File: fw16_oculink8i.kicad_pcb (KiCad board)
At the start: 4 copper layers, 118.7 x 72.5 mm, 18 parts, among them J1 173162-0131, J3 Fan0, J4 Fan1, U1 BR24G32FVT-3GE2

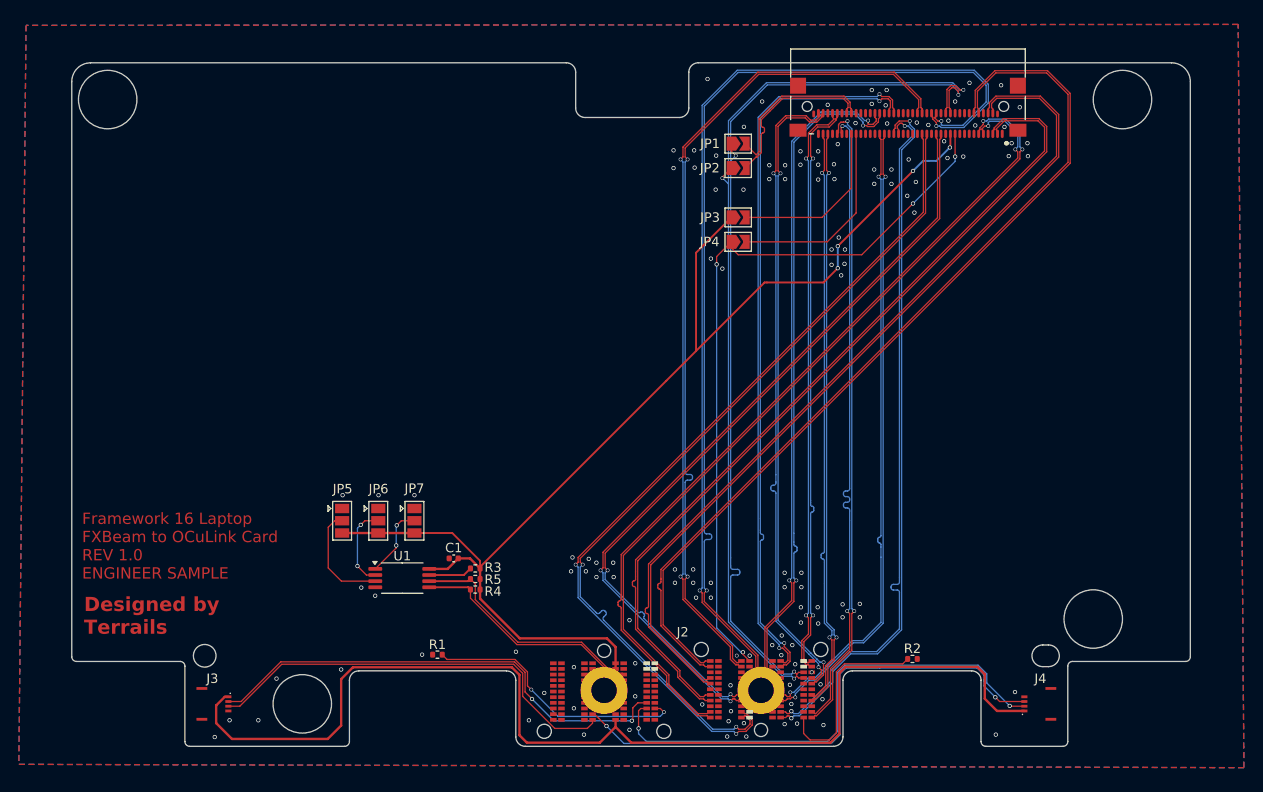
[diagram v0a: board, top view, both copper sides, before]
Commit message: Switch to 0R resistor rather than jumper solder pads
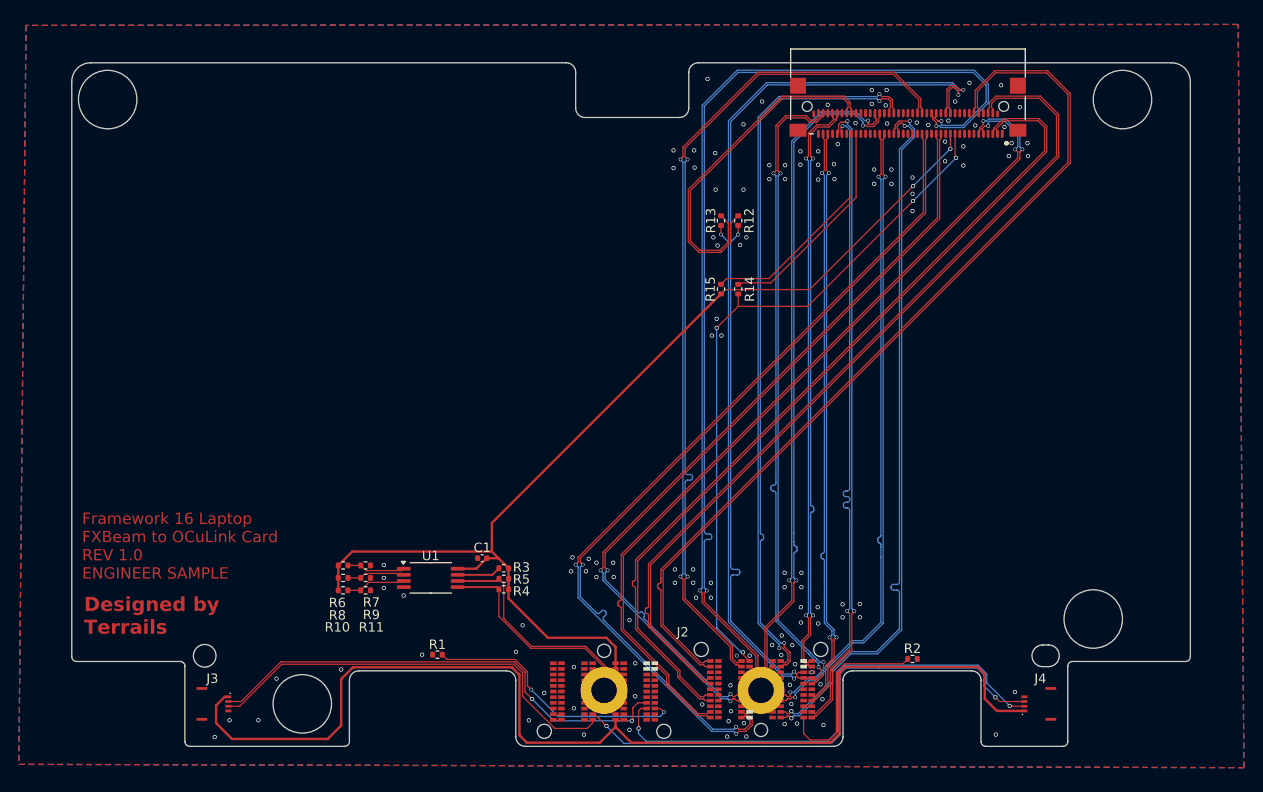
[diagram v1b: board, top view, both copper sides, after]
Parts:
- removed JP1: CLK+ Bridge, Jumper:SolderJumper-2_P1.3mm_Open_TrianglePad1.0x1.5mm
- removed JP2: CLK- Bridge, Jumper:SolderJumper-2_P1.3mm_Open_TrianglePad1.0x1.5mm
- removed JP3: CPRSNT Bridge, Jumper:SolderJumper-2_P1.3mm_Open_TrianglePad1.0x1.5mm
- removed JP4: PERST Bridge, Jumper:SolderJumper-2_P1.3mm_Open_TrianglePad1.0x1.5mm
- removed JP5: A2 Bridge, Jumper:SolderJumper-3_P1.3mm_Open_Pad1.0x1.5mm
- removed JP6: A1 Bridge, Jumper:SolderJumper-3_P1.3mm_Open_Pad1.0x1.5mm
- removed JP7: A0 Bridge, Jumper:SolderJumper-3_P1.3mm_Open_Pad1.0x1.5mm
- added R10: 0R, Resistor_SMD:R_0402_1005Metric, F.Cu at (71.9, 80.6)
- added R11: 0R, Resistor_SMD:R_0402_1005Metric, F.Cu at (74.3, 80.6)
- added R12: 0R, Resistor_SMD:R_0402_1005Metric, F.Cu at (113.8, 41.4)
- added R13: 0R, Resistor_SMD:R_0402_1005Metric, F.Cu at (112.0, 41.4)
- added R14: 0R, Resistor_SMD:R_0402_1005Metric, F.Cu at (113.8, 48.7)
- added R15: 0R, Resistor_SMD:R_0402_1005Metric, F.Cu at (112.0, 48.7)
- added R6: 0R, Resistor_SMD:R_0402_1005Metric, F.Cu at (71.9, 78.0)
- added R7: 0R, Resistor_SMD:R_0402_1005Metric, F.Cu at (74.3, 78.0)
- added R8: 0R, Resistor_SMD:R_0402_1005Metric, F.Cu at (71.9, 79.3)
- added R9: 0R, Resistor_SMD:R_0402_1005Metric, F.Cu at (74.3, 79.3)
- moved C1 3.02 mm to (86.6, 77.2)
- moved R3 3.02 mm to (88.9, 78.3)
- moved R4 3.02 mm to (88.9, 80.5)
- moved R5 3.02 mm to (88.9, 79.4)
- moved U1 3.02 mm to (81.2, 79.3)
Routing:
- net /REFCLKB+: track 17.8 -> 36.9 mm
- net /REFCLKB-: track 17.7 -> 35.3 mm
- net 3V3_ALW: track 132.1 -> 115.5 mm, vias 4 -> 2
- net /CPRSNTB: track 18.3 -> 24.3 mm
- net /A2: track 11.6 -> 6.34 mm
- net /PERSTA: track 78.4 -> 73.7 mm
- net /A1: track 8.83 -> 6.18 mm, vias 2 -> 0
- net /I2C_SDA: track 25.2 -> 23.4 mm
- net /I2C_SCL: track 25.9 -> 24.1 mm
- net /PERSTB: track 21.4 -> 23.1 mm
- net /A0: track 7.64 -> 6.23 mm, vias 2 -> 0
- net GND: vias 133 -> 132

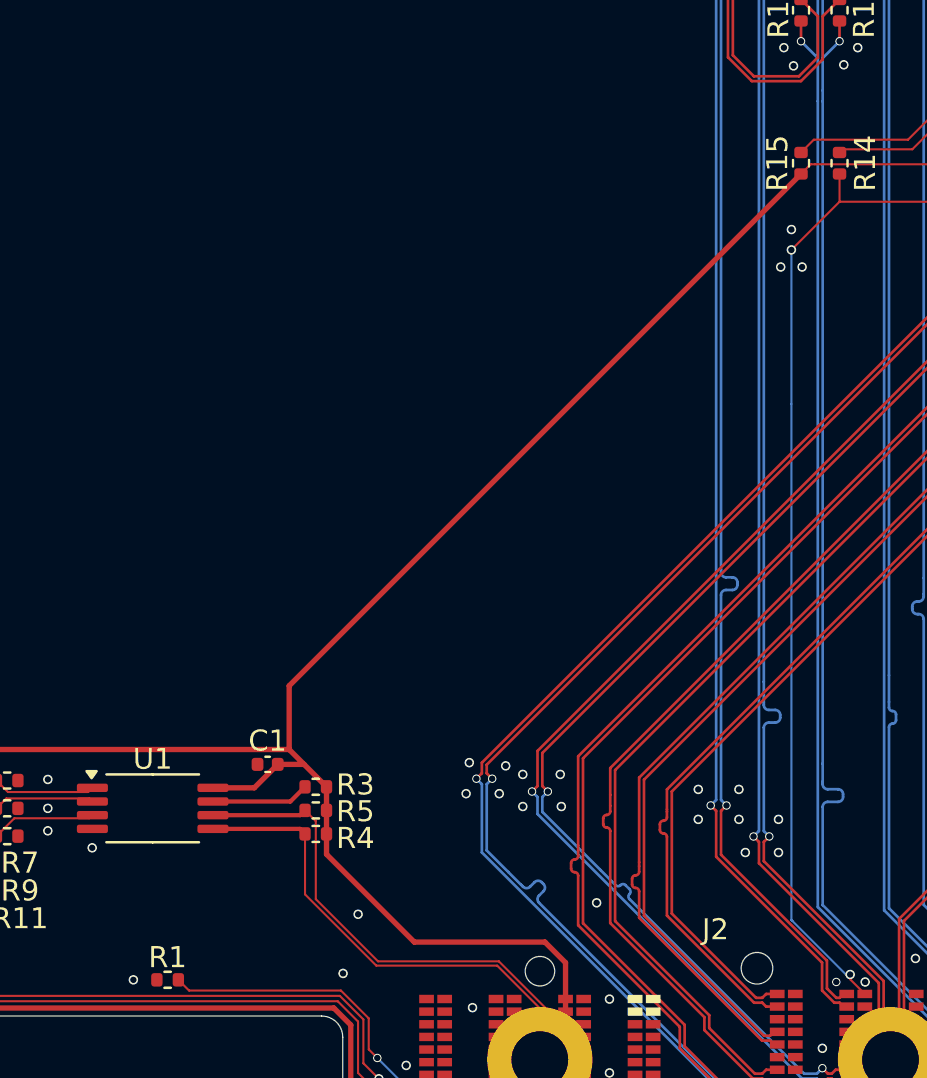
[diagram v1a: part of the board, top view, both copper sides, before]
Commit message: Change resistor numbering
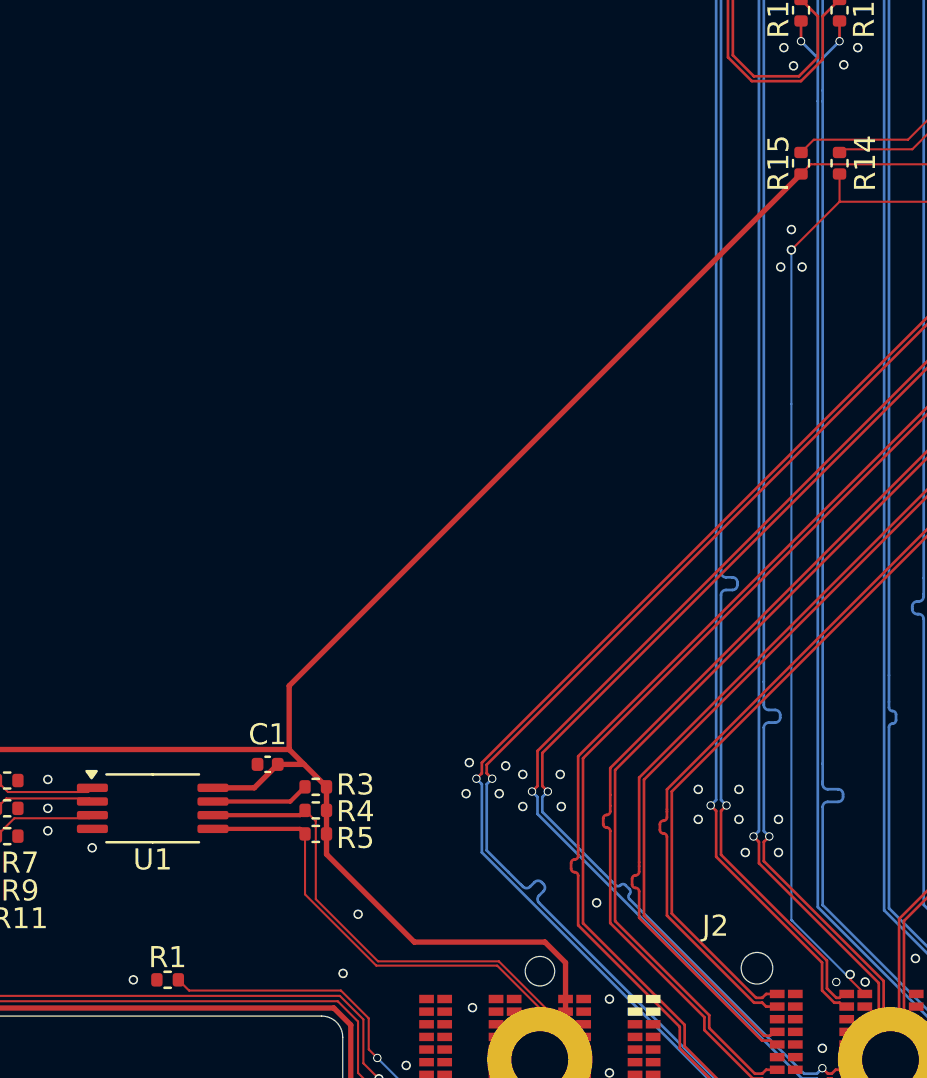
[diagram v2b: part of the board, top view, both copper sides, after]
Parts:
- renumbered R5 to R4, R4 to R5
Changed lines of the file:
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@@
 		(descr "Resistor SMD 0402 (1005 Metric), square (rectangular) end terminal, IPC-7351 nominal, (Body size source: IPC-SM-782 page 72, https://www.pcb-3d.com/wordpress/wp-content/uploads/ipc-sm-782a_amendment_1_and_2.pdf), generated with kicad-footprint-generator")
 		(tags "resistor")
-		(property "Reference" "R5"
+		(property "Reference" "R4"
 			(at -1.8796 -0.0508 180)
 			(layer "F.SilkS")
@@
 		(tags "capacitor")
 		(property "Reference" "C1"
-			(at 0 1.1176 180)
+			(at 0 1.4175 180)
 			(layer "F.SilkS")
 			(effects
@@
 		(at 107.892214 91.231826)
 		(property "Reference" "J2"
-			(at 0.004353 -6.177659 0)
+			(at 0.006986 -6.345026 0)
 			(unlocked yes)
 			(layer "F.SilkS")
@@
 		(tags "resistor")
 		(property "Reference" "R15"
-			(at 0 1.1176 90)
+			(at 0 1.0668 90)
 			(layer "F.SilkS")
 			(effects
@@
 		(descr "Resistor SMD 0402 (1005 Metric), square (rectangular) end terminal, IPC-7351 nominal, (Body size source: IPC-SM-782 page 72, https://www.pcb-3d.com/wordpress/wp-content/uploads/ipc-sm-782a_amendment_1_and_2.pdf), generated with kicad-footprint-generator")
 		(tags "resistor")
-		(property "Reference" "R4"
+		(property "Reference" "R5"
 			(at 1.8796 0.2032 180)
 			(layer "F.SilkS")
@@
 		(tags "TSSOP SO")
 		(property "Reference" "U1"
-			(at 0 -2.3417 0)
+			(at 0 2.4384 0)
 			(layer "F.SilkS")
 			(effects
@@
 			(at 0 2.4335 0)
 			(layer "F.Fab")
+			(hide yes)
 			(effects
 				(font

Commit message: schematic cleanup
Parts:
- J1: renamed from J2; value ~ -> FXBeam
- renumbered J3 to J2, J4 to J3, J1 to J4
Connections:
- net Net-(J2-12V_FAN) renamed 12V_FAN
- net Net-(J2-Fan0_PWM) renamed /FAN0_PWM
- net Net-(J2-Fan0_SPEED) renamed /FAN0_SPD
- net Net-(J2-Fan1_PWM) renamed /FAN1_PWM
- net Net-(J2-Fan1_SPEED) renamed /FAN1_SPD
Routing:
- net /A0: track 6.23 -> 7.09 mm
- net /A2: track 6.34 -> 7.07 mm
- net /A1: track 6.18 -> 6.91 mm
- net GND: vias 132 -> 133

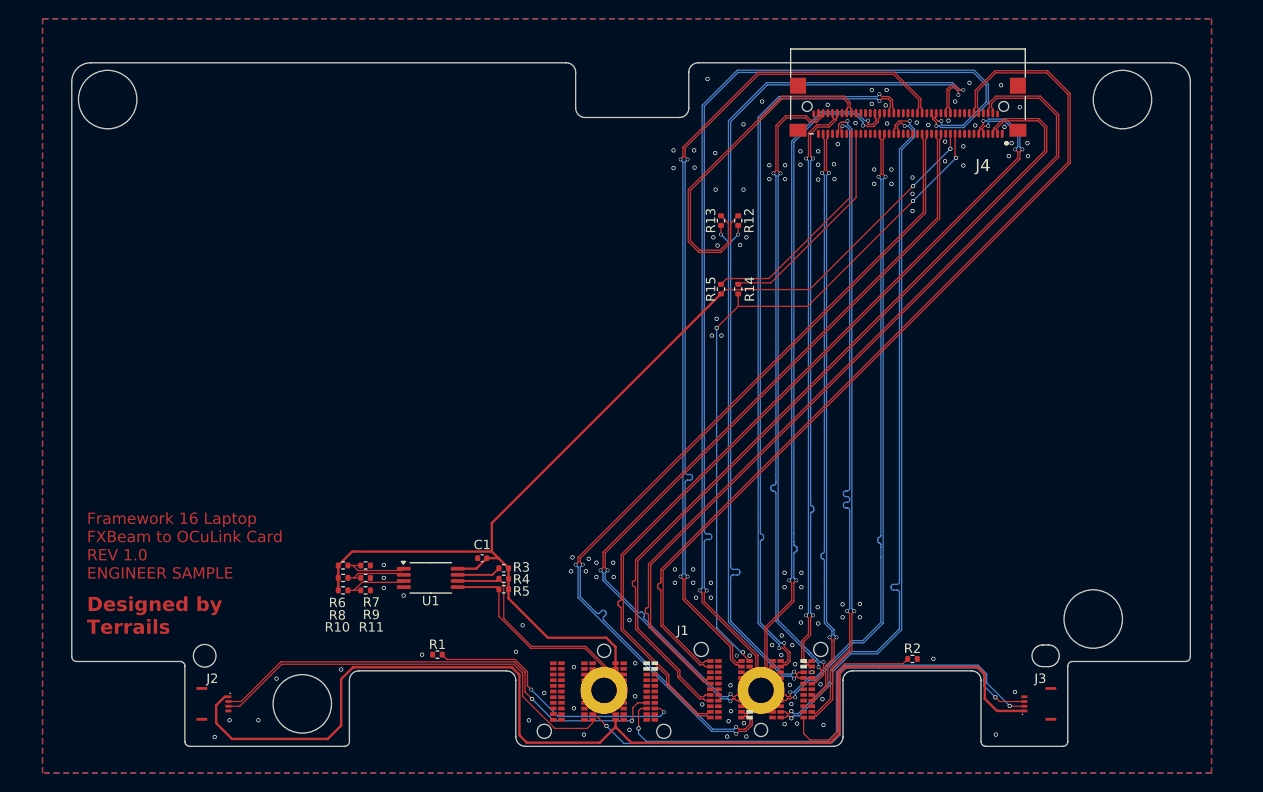
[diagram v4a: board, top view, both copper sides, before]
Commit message: Add R0 resistors to EEPROM power supply
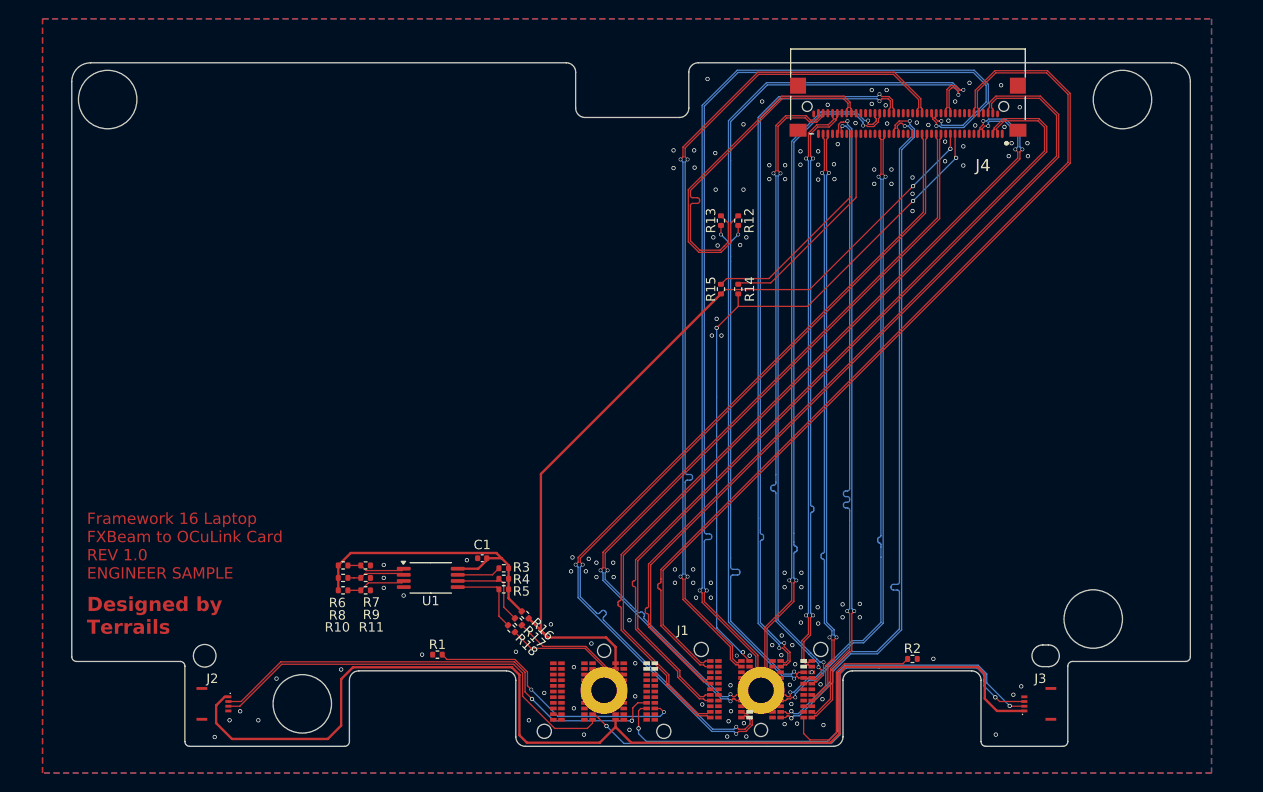
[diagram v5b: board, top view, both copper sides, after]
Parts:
- added R16: 0R, Resistor_SMD:R_0402_1005Metric, F.Cu at (91.2, 83.2)
- added R17: 0R, Resistor_SMD:R_0402_1005Metric, F.Cu at (90.5, 83.9)
- added R18: 0R, Resistor_SMD:R_0402_1005Metric, F.Cu at (89.7, 84.7)
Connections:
- C1 pad 1: 3V3_ALW -> /3V3_EEPROM
- R10 pad 1: 3V3_ALW -> /3V3_EEPROM
- R3 pad 1: 3V3_ALW -> /3V3_EEPROM
- R4 pad 1: 3V3_ALW -> /3V3_EEPROM
- R4 pad 2: /I2C_SCL -> Net-(U1-SCL)
- R5 pad 1: /I2C_SDA -> Net-(U1-SDA)
- R5 pad 2: 3V3_ALW -> /3V3_EEPROM
- R6 pad 1: 3V3_ALW -> /3V3_EEPROM
- R8 pad 1: 3V3_ALW -> /3V3_EEPROM
- U1 pad 5: /I2C_SDA -> Net-(U1-SDA)
- U1 pad 6: /I2C_SCL -> Net-(U1-SCL)
- U1 pad 8: 3V3_ALW -> /3V3_EEPROM
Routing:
- net /3V3_EEPROM: track 0.00 -> 32.5 mm
- net 3V3_ALW: track 115.5 -> 89.8 mm
- net /I2C_SCL: track 24.1 -> 13.0 mm
- net /I2C_SDA: track 23.4 -> 13.7 mm
- net Net-(U1-SCL): track 0.00 -> 9.36 mm
- net Net-(U1-SDA): track 0.00 -> 8.68 mm
- net /REFCLKB-: track 35.3 -> 36.8 mm
- net /A0: track 7.09 -> 6.23 mm
- net /A2: track 7.07 -> 6.34 mm
- net /A1: track 6.91 -> 6.18 mm
- net GND: vias 133 -> 137
